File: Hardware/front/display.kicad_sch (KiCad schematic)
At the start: 12 parts

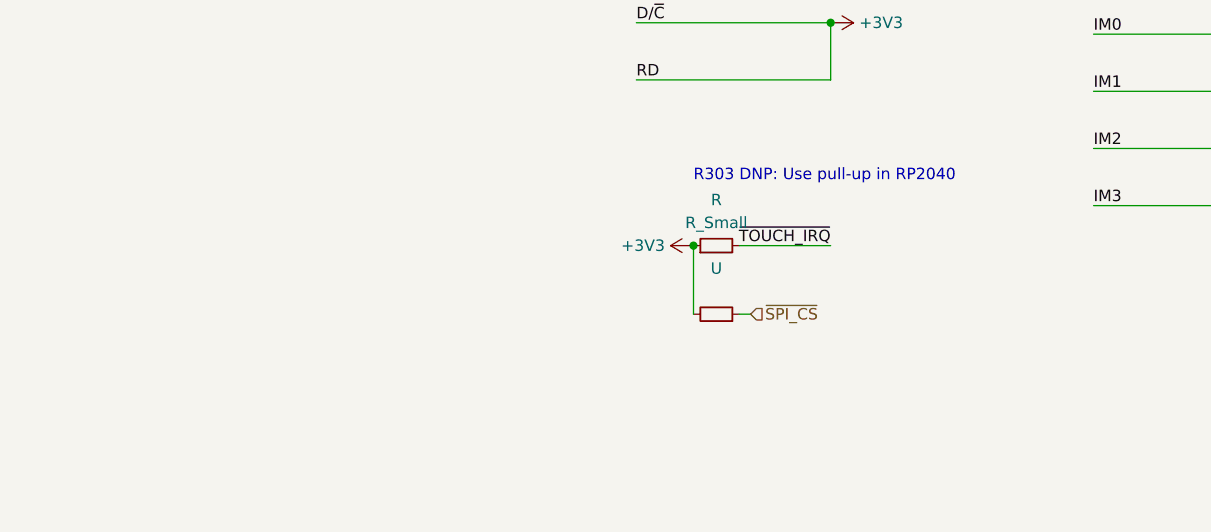
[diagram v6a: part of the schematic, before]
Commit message: updated front panel pinout
- added system reset, direct load on/off switch output lines

- added separate touch screen reset/interrupt lines (the touch
  controller gets to be driven by linux side)

- update footprint for ER-TFT040-1 display

  this tweaks the sizes of the openings and the text labels a bit to be
  prettier
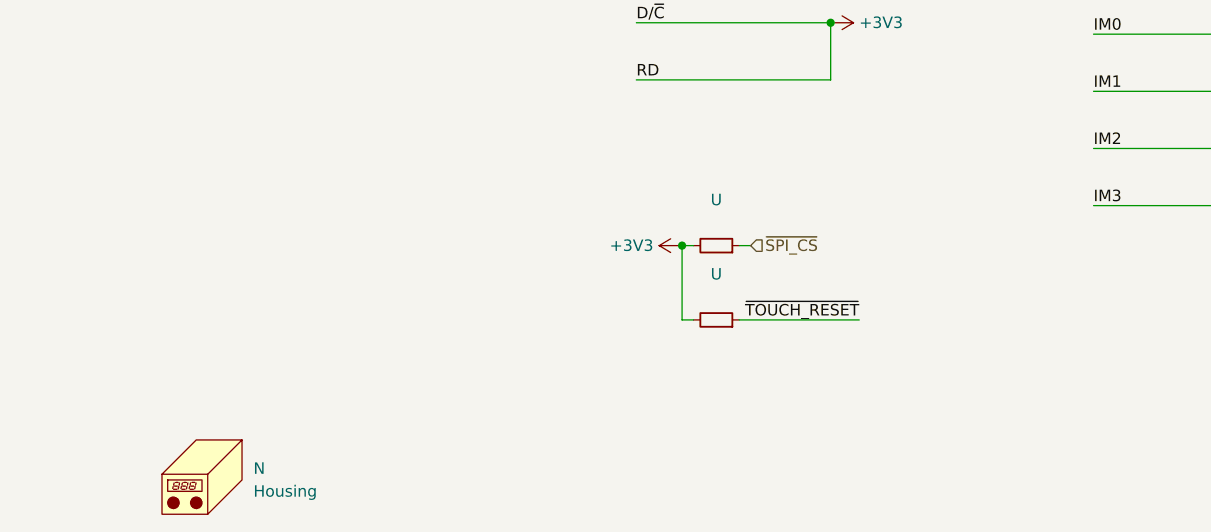
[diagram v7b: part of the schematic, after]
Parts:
- removed R: R_Small, symbol Device:R_Small
- added N: Housing, symbol Mechanical:Housing
- added U: (no value), symbol Device:R_Small
- J: JLCPCB (none) -> C231436
- R, U: JLCPCB (none) -> C25804
- U: JLCPCB (none) -> C14663
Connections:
- net +3V3: now also U.2
- net ~{TOUCH_RESET}: now also U.1
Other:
- note removed: "R303 DNP: Use pull-up in RP2040"
- moved on the sheet: U
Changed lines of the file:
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@@
   (junction (at 267.97 46.99) (diameter 0) (color 0 0 0 0)
   )
+  (junction (at 199.39 146.05) (diameter 0) (color 0 0 0 0)
+  )
   (junction (at 217.17 31.75) (diameter 0) (color 0 0 0 0)
   )
@@
   (junction (at 267.97 52.07) (diameter 0) (color 0 0 0 0)
   )
-  (junction (at 200.66 146.05) (diameter 0) (color 0 0 0 0)
-  )
   (junction (at 266.7 141.605) (diameter 0) (color 0 0 0 0)
   )
@@
     (stroke (width 0) (type default))
   )
+  (wire (pts (xy 199.39 146.05) (xy 199.39 154.305))
+    (stroke (width 0) (type default))
+  )
   (wire (pts (xy 229.87 69.85) (xy 240.03 69.85))
     (stroke (width 0) (type default))
@@
     (stroke (width 0) (type default))
   )
+  (wire (pts (xy 205.74 154.305) (xy 219.075 154.305))
+    (stroke (width 0) (type default))
+  )
   (wire (pts (xy 215.9 49.53) (xy 217.17 49.53))
     (stroke (width 0) (type default))
@@
     (stroke (width 0) (type default))
   )
-  (wire (pts (xy 205.74 146.05) (xy 215.9 146.05))
-    (stroke (width 0) (type default))
-  )
   (wire (pts (xy 215.9 57.15) (xy 217.17 57.15))
     (stroke (width 0) (type default))
   )
-  (wire (pts (xy 205.74 153.67) (xy 207.01 153.67))
+  (wire (pts (xy 205.74 146.05) (xy 207.01 146.05))
     (stroke (width 0) (type default))
   )
@@
     (stroke (width 0) (type default))
   )
-  (wire (pts (xy 200.66 146.05) (xy 200.66 153.67))
-    (stroke (width 0) (type default))
-  )
   (bus (pts (xy 242.57 67.31) (xy 243.84 67.31))
     (stroke (width 0) (type default))
@@
     (stroke (width 0) (type default))
   )
+  (wire (pts (xy 199.39 146.05) (xy 200.66 146.05))
+    (stroke (width 0) (type default))
+  )
   (wire (pts (xy 207.01 87.63) (xy 217.17 87.63))
     (stroke (width 0) (type default))
@@
     (stroke (width 0) (type default))
   )
+  (wire (pts (xy 199.39 154.305) (xy 200.66 154.305))
+    (stroke (width 0) (type default))
+  )
   (bus (pts (xy 242.57 67.31) (xy 242.57 69.85))
     (stroke (width 0) (type default))
@@
   )
   (text "For ER-TFT040-1 display" (at 203.835 21.59 0)
-    (effects (font (size 1.27 1.27)) (justify left bottom))
-  )
-  (text "R303 DNP: Use pull-up in RP2040" (at 200.66 139.065 0)
     (effects (font (size 1.27 1.27)) (justify left bottom))
   )
@@
     (effects (font (size 1.27 1.27)) (justify left bottom))
   )
+  (label "~{TOUCH_RESET}" (at 219.075 154.305 180) (fields_autoplaced)
+    (effects (font (size 1.27 1.27)) (justify right bottom))
+  )
   (label "IM2" (at 245.11 135.255 0) (fields_autoplaced)
     (effects (font (size 1.27 1.27)) (justify left bottom))
-  )
-  (label "~{TOUCH_IRQ}" (at 215.9 146.05 0) (fields_autoplaced)
-    (effects (font (size 1.27 1.27)) (justify right bottom))
   )
   (label "R2" (at 217.17 72.39 0) (fields_autoplaced)
@@
     (effects (font (size 1.27 1.27)) (justify left))
   )
-  (hierarchical_label "~{SPI_CS}" (shape input) (at 207.01 153.67 0) (fields_autoplaced)
-    (effects (font (size 1.27 1.27)) (justify left))
-  )
-  (symbol (lib_id "Device:R_Small") (at 203.2 146.05 90) (unit 1)
-    (in_bom no) (on_board no) (fields_autoplaced)
-    (default_instance (reference "R") (unit 1) (value "R_Small") (footprint ""))
-    (property "Reference" "R" (id 0) (at 203.2 140.97 90)
-      (effects (font (size 1.27 1.27)))
-    )
-    (property "Value" "R_Small" (id 1) (at 203.2 143.51 90)
-      (effects (font (size 1.27 1.27)))
-    )
-    (property "Footprint" "" (id 2) (at 203.2 146.05 0)
-      (effects (font (size 1.27 1.27)) hide)
-    )
-    (property "Datasheet" "~" (id 3) (at 203.2 146.05 0)
-      (effects (font (size 1.27 1.27)) hide)
-    )
-    (pin "1")
-    (pin "2")
+  (hierarchical_label "~{SPI_CS}" (shape input) (at 207.01 146.05 0) (fields_autoplaced)
+    (effects (font (size 1.27 1.27)) (justify left))
   )
   (symbol (lib_id "Device:C_Small") (at 257.175 49.53 0) (unit 1)
@@
       (effects (font (size 1.27 1.27)) hide)
     )
+    (property "JLCPCB" "C14663" (id 5) (at 257.175 49.53 0)
+      (effects (font (size 1.27 1.27)) hide)
+    )
     (pin "1")
     (pin "2")
@@
     (pin "3")
   )
+  (symbol (lib_id "Mechanical:Housing") (at 147.32 171.45 0) (unit 1)
+    (in_bom yes) (on_board yes)
+    (default_instance (reference "N") (unit 1) (value "Housing") (footprint ""))
+    (property "Reference" "N" (id 0) (at 151.765 170.815 0)
+      (effects (font (size 1.27 1.27)) (justify left))
+    )
+    (property "Value" "Housing" (id 1) (at 151.765 173.355 0)
+      (effects (font (size 1.27 1.27)) (justify left))
+    )
+    (property "Footprint" "" (id 2) (at 148.59 170.18 0)
+      (effects (font (size 1.27 1.27)) hide)
+    )
+    (property "Datasheet" "~" (id 3) (at 148.59 170.18 0)
+      (effects (font (size 1.27 1.27)) hide)
+    )
+  )
+  (symbol (lib_id "Device:R_Small") (at 203.2 154.305 270) (mirror x) (unit 1)
+    (in_bom yes) (on_board yes)
+    (default_instance (reference "U") (unit 1) (value "") (footprint ""))
+    (property "Reference" "U" (id 0) (at 203.2 149.225 90)
+      (effects (font (size 1.27 1.27)))
+    )
+    (property "Value" "" (id 1) (at 203.2 151.765 90)
+      (effects (font (size 1.27 1.27)))
+    )
+    (property "Footprint" "" (id 2) (at 203.2 154.305 0)
+      (effects (font (size 1.27 1.27)) hide)
+    )
+    (property "Datasheet" "~" (id 3) (at 203.2 154.305 0)
+      (effects (font (size 1.27 1.27)) hide)
+    )
+    (property "MPN" "" (id 4) (at 203.2 154.305 90)
+      (effects (font (size 1.27 1.27)) hide)
+    )
+    (property "JLCPCB" "C25804" (id 5) (at 203.2 154.305 90)
+      (effects (font (size 1.27 1.27)) hide)
+    )
+    (pin "1")
+    (pin "2")
+  )
   (symbol (lib_id "power:+3V3") (at 267.97 46.99 0) (unit 1)
     (in_bom yes) (on_board yes) (fields_autoplaced)
@@
     (pin "1")
   )
-  (symbol (lib_id "Device:R_Small") (at 203.2 153.67 270) (mirror x) (unit 1)
+  (symbol (lib_id "Device:R_Small") (at 203.2 146.05 270) (mirror x) (unit 1)
     (in_bom yes) (on_board yes)
     (default_instance (reference "U") (unit 1) (value "") (footprint ""))
-    (property "Reference" "U" (id 0) (at 203.2 148.59 90)
-      (effects (font (size 1.27 1.27)))
-    )
-    (property "Value" "" (id 1) (at 203.2 151.13 90)
-      (effects (font (size 1.27 1.27)))
-    )
-    (property "Footprint" "" (id 2) (at 203.2 153.67 0)
-      (effects (font (size 1.27 1.27)) hide)
-    )
-    (property "Datasheet" "~" (id 3) (at 203.2 153.67 0)
-      (effects (font (size 1.27 1.27)) hide)
-    )
-    (property "MPN" "" (id 4) (at 203.2 153.67 90)
+    (property "Reference" "U" (id 0) (at 203.2 140.97 90)
+      (effects (font (size 1.27 1.27)))
+    )
+    (property "Value" "" (id 1) (at 203.2 143.51 90)
+      (effects (font (size 1.27 1.27)))
+    )
+    (property "Footprint" "" (id 2) (at 203.2 146.05 0)
+      (effects (font (size 1.27 1.27)) hide)
+    )
+    (property "Datasheet" "~" (id 3) (at 203.2 146.05 0)
+      (effects (font (size 1.27 1.27)) hide)
+    )
+    (property "MPN" "" (id 4) (at 203.2 146.05 90)
+      (effects (font (size 1.27 1.27)) hide)
+    )
+    (property "JLCPCB" "C25804" (id 5) (at 203.2 146.05 90)
       (effects (font (size 1.27 1.27)) hide)
     )
@@
     (pin "1")
   )
-  (symbol (lib_id "power:+3V3") (at 200.66 146.05 90) (unit 1)
+  (symbol (lib_id "power:+3V3") (at 199.39 146.05 90) (unit 1)
     (in_bom yes) (on_board yes)
     (default_instance (reference "#PWR") (unit 1) (value "+3V3") (footprint ""))
-    (property "Reference" "#PWR" (id 0) (at 204.47 146.05 0)
-      (effects (font (size 1.27 1.27)) hide)
-    )
-    (property "Value" "+3V3" (id 1) (at 197.485 146.05 90)
-      (effects (font (size 1.27 1.27)) (justify left))
-    )
-    (property "Footprint" "" (id 2) (at 200.66 146.05 0)
-      (effects (font (size 1.27 1.27)) hide)
-    )
-    (property "Datasheet" "" (id 3) (at 200.66 146.05 0)
+    (property "Reference" "#PWR" (id 0) (at 203.2 146.05 0)
+      (effects (font (size 1.27 1.27)) hide)
+    )
+    (property "Value" "+3V3" (id 1) (at 196.215 146.05 90)
+      (effects (font (size 1.27 1.27)) (justify left))
+    )
+    (property "Footprint" "" (id 2) (at 199.39 146.05 0)
+      (effects (font (size 1.27 1.27)) hide)
+    )
+    (property "Datasheet" "" (id 3) (at 199.39 146.05 0)
       (effects (font (size 1.27 1.27)) hide)
     )
@@
       (effects (font (size 1.27 1.27)) hide)
     )
+    (property "JLCPCB" "C25804" (id 4) (at 50.8 76.2 90)
+      (effects (font (size 1.27 1.27)) hide)
+    )
     (pin "1")
     (pin "2")
@@
       (effects (font (size 1.27 1.27)) hide)
     )
+    (property "JLCPCB" "C231436" (id 4) (at 222.25 59.69 0)
+      (effects (font (size 1.27 1.27)) hide)
+    )
